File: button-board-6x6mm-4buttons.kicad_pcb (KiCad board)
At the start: 2 copper layers, 52 x 20 mm, 23 parts, among them J1 Conn_02x03_Counter_Clockwise, SW1 SW_Push, SW2 SW_Push, SW3 SW_Push, SW4 SW_Push

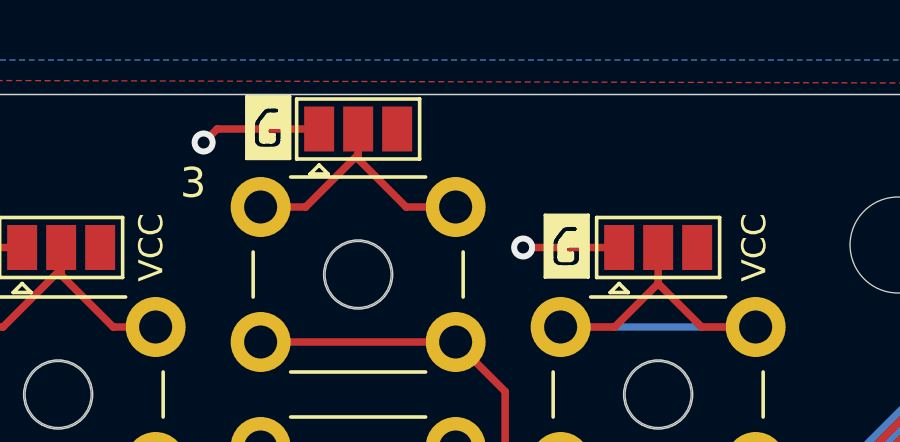
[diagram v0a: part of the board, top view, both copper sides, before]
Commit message: silkscreen minor update
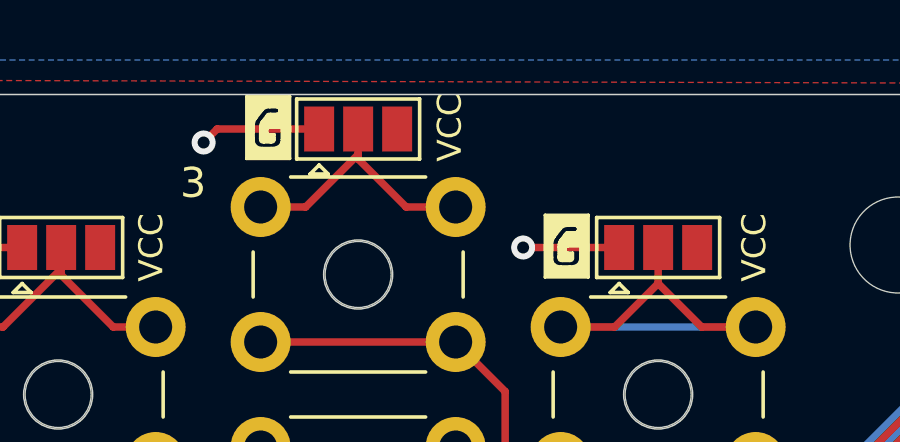
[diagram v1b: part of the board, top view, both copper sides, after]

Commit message: update to v1r1
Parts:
- removed the REF** at (55.5, 33.1)
- removed the REF** at (55.5, 50.9)
- added REF**: SYM_G_SilkScreen_Front, zytzeiche:SYM_G_SilkScreen_Front, B.Cu at (47.4, 35.8)
- added REF**: SYM_G_SilkScreen_Front, zytzeiche:SYM_G_SilkScreen_Front, B.Cu at (47.1, 48.3)
- J1: value Conn_02x03_Counter_Clockwise -> Conn_01x06_Male; footprint Connector_PinSocket_2.54mm:PinSocket_2x03_P2.54mm_Vertical -> Connector_PinSocket_2.54mm:PinSocket_1x06_P2.54mm_Vertical
- JP1, JP2, JP3, JP4, REF** (x2): moved to B.Cu
- moved JP2 8.65 mm to (50.2, 48.2)
- moved JP1 8.52 mm to (40.5, 39.8)
- moved JP3 8.46 mm to (50.5, 35.8)
- moved REF** 8.40 mm to (37.5, 39.8), turned to 180 degrees
- moved REF** 7.14 mm to (81.2, 48.4), turned to 0 degrees
- moved REF** 6.87 mm to (81.5, 48.4), turned to 0 degrees
- moved J1 3.88 mm to (84.6, 35.6)
- moved H1 1.00 mm to (40.5, 36.0)
- moved H5 1.00 mm to (76.5, 36.0)
- moved H7 1.00 mm to (40.5, 48.0)
- moved H8 1.00 mm to (76.5, 48.0)
- turned REF** to 180 degrees
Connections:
- J1 pad 1: VCC -> Net-(J1-Pad1)
- J1 pad 5: GND -> VCC
- J1 pad 6: Net-(J1-Pad6) -> GND
- SW1 pad 2: Net-(J1-Pad2) -> Net-(J1-Pad1)
- SW2 pad 2: Net-(J1-Pad4) -> Net-(J1-Pad2)
- SW3 pad 2: Net-(J1-Pad6) -> Net-(J1-Pad3)
- SW4 pad 2: Net-(J1-Pad3) -> Net-(J1-Pad4)
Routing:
- net Net-(J1-Pad1): track 0.00 -> 43.5 mm
- net Net-(J1-Pad6): track 39.7 -> 0.00 mm
- net GND: track 15.0 -> 0.00 mm, vias 6 -> 0
- net Net-(J1-Pad2): track 46.8 -> 35.4 mm
- net Net-(J1-Pad4): track 29.9 -> 19.8 mm
- net VCC: track 0.00 -> 8.25 mm, vias 0 -> 4
- net Net-(JP1-Pad2): track 9.65 -> 14.2 mm
- net Net-(JP3-Pad2): track 8.89 -> 13.2 mm
- net Net-(JP4-Pad2): track 15.4 -> 11.7 mm
- net Net-(J1-Pad3): track 27.6 -> 30.5 mm
- net Net-(JP2-Pad2): track 15.0 -> 14.4 mm
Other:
- board text added: "- 3 buttons (6x6) - 52x20mm - holes d=3.2mm, distance=36mm and 12mm"
- board text added: "4 buttons (6x6), 52x20mm, M3 holes d=3.2mm, distance=36/12mm"
- board text added: "Btn1"
- board text added: "Btn2"
- board text added: "Btn3"
- board text added: "Btn4"
- board text added: "M3"
- board text added: "bb-6x6-4b v1r1"
- board text removed: "- 3 buttons (6x6) - 52x20mm - holes d=3.2mm, distance=36mm and 10mm"
- board text removed: "3 buttons (6x6), 52x12mm, holes d=3.3mm, distance=36/10mm"

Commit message: SilkScreen correction
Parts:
- added REF**: SYM_HK_SilkScreen_Back, user-footprints:SYM_HK_SilkScreen_Back, F.Cu at (79.7, 39.2)
- added REF**: Sig_Keltenberg-B.SilkS, user-footprints:Sig_Keltenberg-B.SilkS, F.Cu at (73.1, 43.2)
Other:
- board text added: "bb-6x6-4b v1.2"
- board text added: "v1.2 5/2021"
- board text removed: "bb-6x6-4b v1r1"
- board text removed: "v1r1 5/2021"
